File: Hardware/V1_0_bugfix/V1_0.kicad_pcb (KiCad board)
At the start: 2 copper layers, 83 x 54 mm, 86 parts, among them J1 Micro_SD_Card_Det, J10 C, J11 AUDIO, J2 USART2, J3 USB_B_Mini, J4 UART, J5 C, J6 C, J7 C, J8 C, J9 C, P1 SWD, SW3 BOOT0, U1 LM27762, U2 REF3030, U3 MCP16311_2, U4 STM32F40X_LQFP64, U5 AD5330, U6 LF356, Y1 8M

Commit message: I found a bug
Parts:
- moved R9 2.51 mm to (148.4, 94.5), turned to 180 degrees
- moved R10 1.47 mm to (148.4, 96.0), turned to 0 degrees
- moved C2 0.37 mm to (145.1, 90.4)
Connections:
- C7 pad 1: /RAIL- -> /DCDC/RAIL-_1
- R10 pad 1: /RAIL- -> GND
- R10 pad 2: GND -> Net-(R10-Pad2)
- R9 pad 1: Net-(R9-Pad1) -> Net-(R10-Pad2)
- R9 pad 2: /RAIL- -> /DCDC/RAIL-_1
- U1 pad 6: /RAIL- -> /DCDC/RAIL-_1
- U1 pad 7: Net-(R9-Pad1) -> Net-(R10-Pad2)
- U6 pad 4: /RAIL- -> /DCDC/RAIL-_1
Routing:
- net /DCDC/RAIL-_1: track 0.00 -> 24.7 mm, vias 0 -> 4
- net /RAIL-: track 20.2 -> 0.00 mm, vias 2 -> 0
- net GND: track 777.0 -> 769.0 mm, vias 132 -> 131
- net Net-(R10-Pad2): track 0.00 -> 5.38 mm
- net +5V: track 87.7 -> 83.7 mm
- net Net-(R9-Pad1): track 2.54 -> 0.00 mm

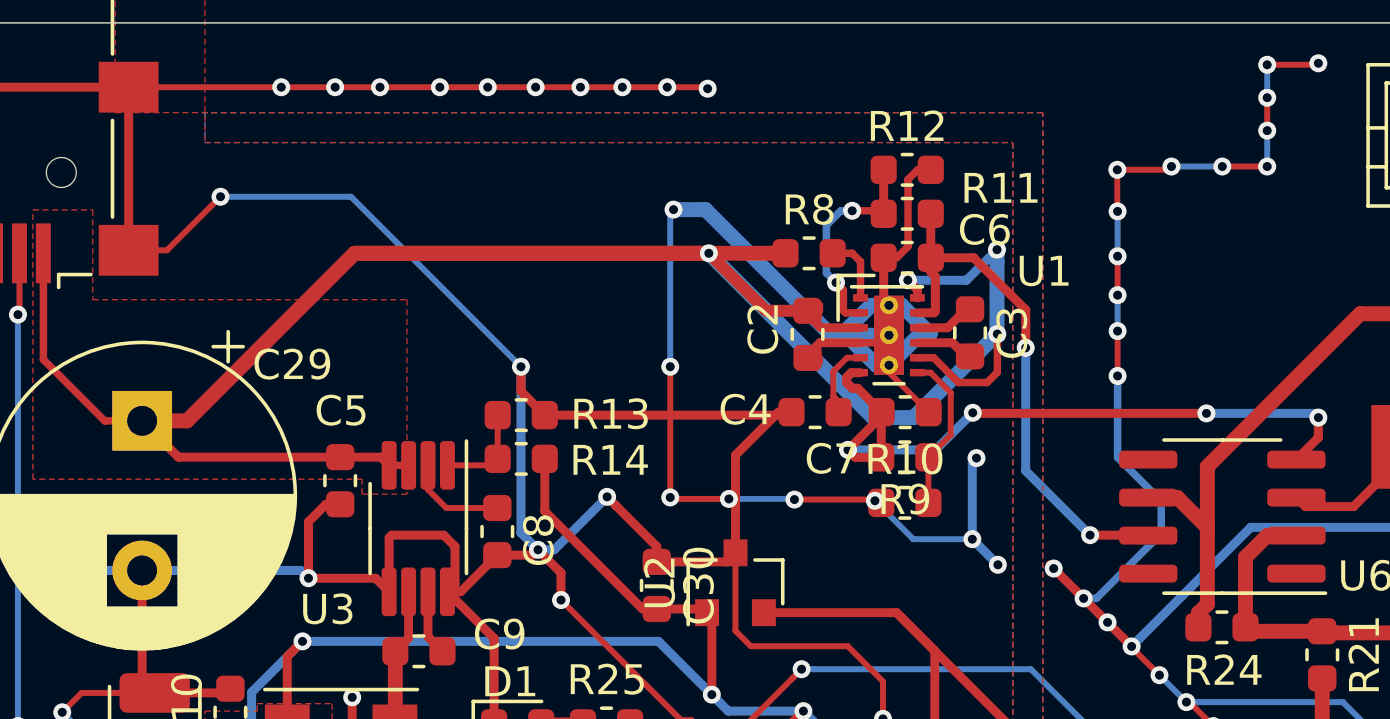
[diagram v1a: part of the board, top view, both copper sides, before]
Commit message: small tweaks to bug fixed version of synth pcb. Also converted to kicad 5.1.5
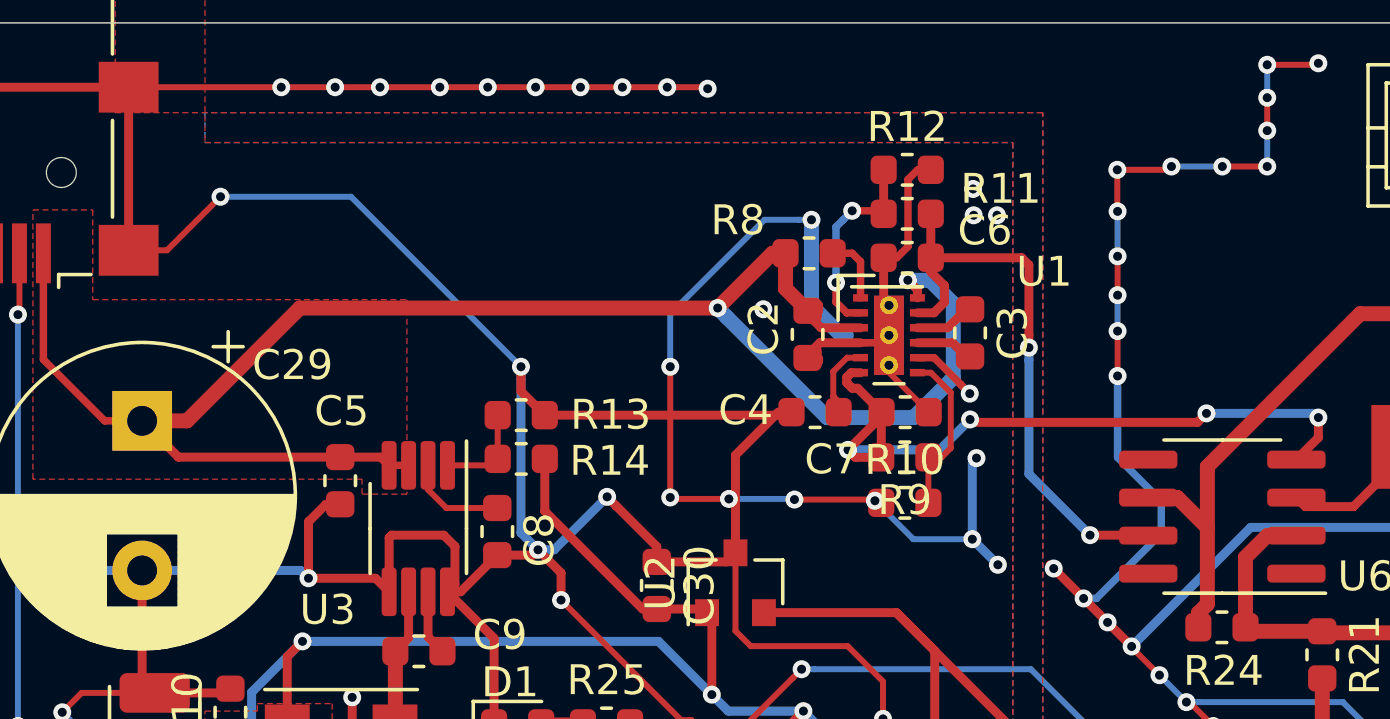
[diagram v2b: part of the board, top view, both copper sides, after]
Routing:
- net +5V: track 83.7 -> 63.6 mm, vias 4 -> 3
- net GND: track 769.0 -> 759.4 mm, vias 131 -> 135
- net /RAIL+: track 18.2 -> 19.4 mm
- net Net-(R11-Pad2): track 7.32 -> 6.81 mm
